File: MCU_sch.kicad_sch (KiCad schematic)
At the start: 10 parts

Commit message: WIP output stage
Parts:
- added R? (x2): 4.7k, symbol Device:R_US
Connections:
- net +3V3: now also R?.1, R?.1
- net DAC_SCL: now reaches IC?.17 (TCK/RPB8/SCL1/CTED10/PMD4/RB8)
- net DAC_SCL: now also R?.2
- net DAC_SDA: now reaches IC?.18 (TDO/RPB9/SDA1/CTED4/PMD3/RB9)
- net DAC_SDA: now also R?.2
- net PCM_BCLK: now reaches IC?.25 (CVREFOUT/AN10/C3INB/RPB14/SCK1/CTED5/PMWR/RB14)
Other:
- moved on the sheet: C?, R?

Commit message: Adding values to output stage
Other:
- title: (none) -> PIC32 Interface
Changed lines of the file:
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@@
 (kicad_sch (version 20211123) (generator eeschema)
   (paper "A4")
+  (title_block
+    (title "PIC32 Interface")
+  )
   (junction (at 27.94 48.26) (diameter 0) (color 0 0 0 0)
   )

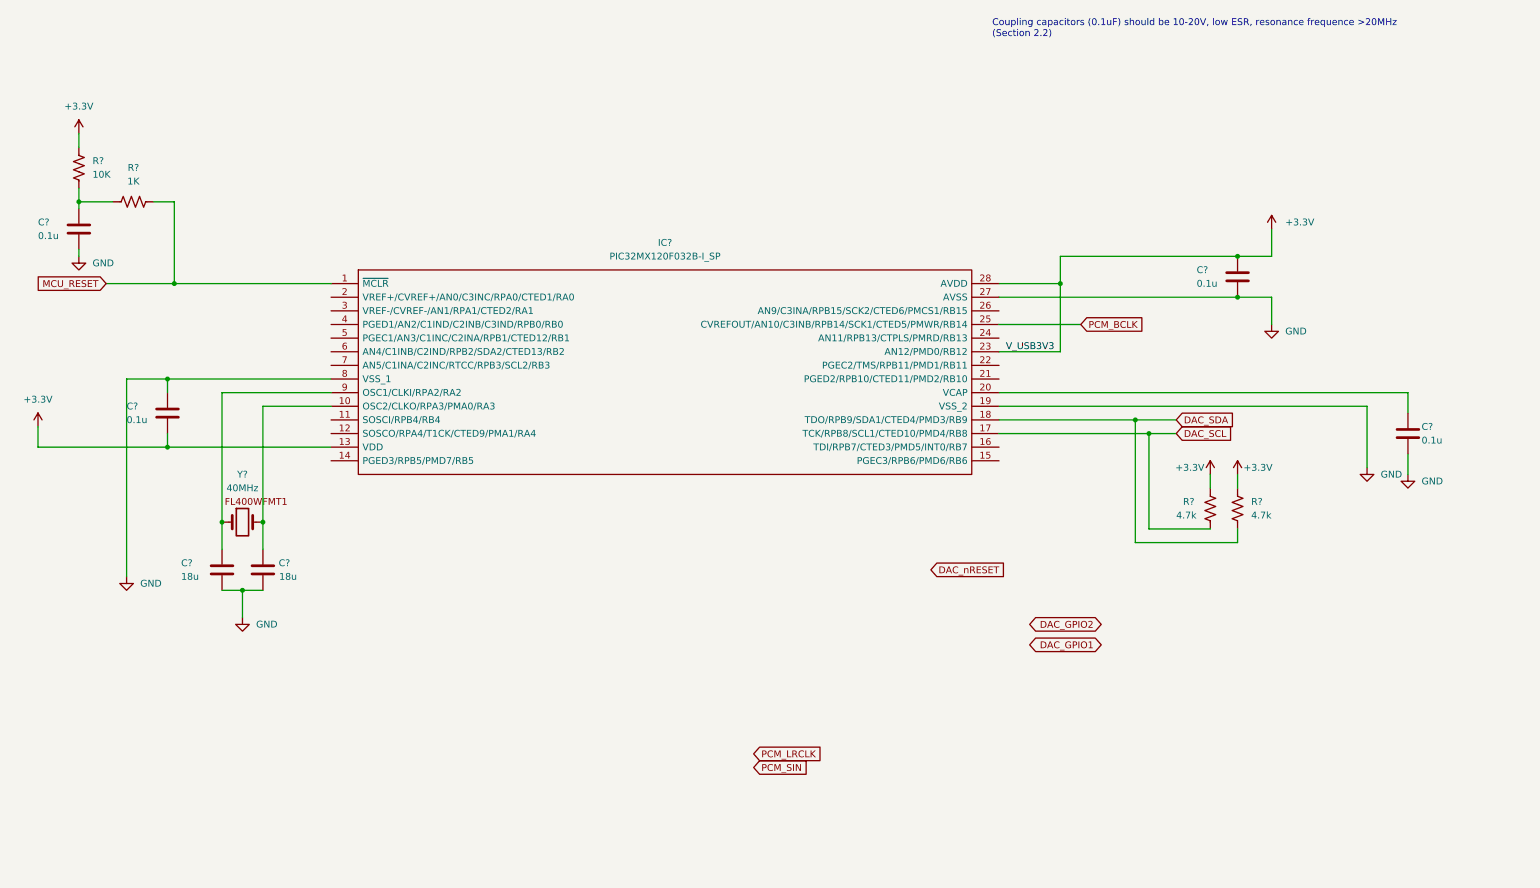
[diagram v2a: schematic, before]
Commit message: Redoing power stage and changing output stage accordingly
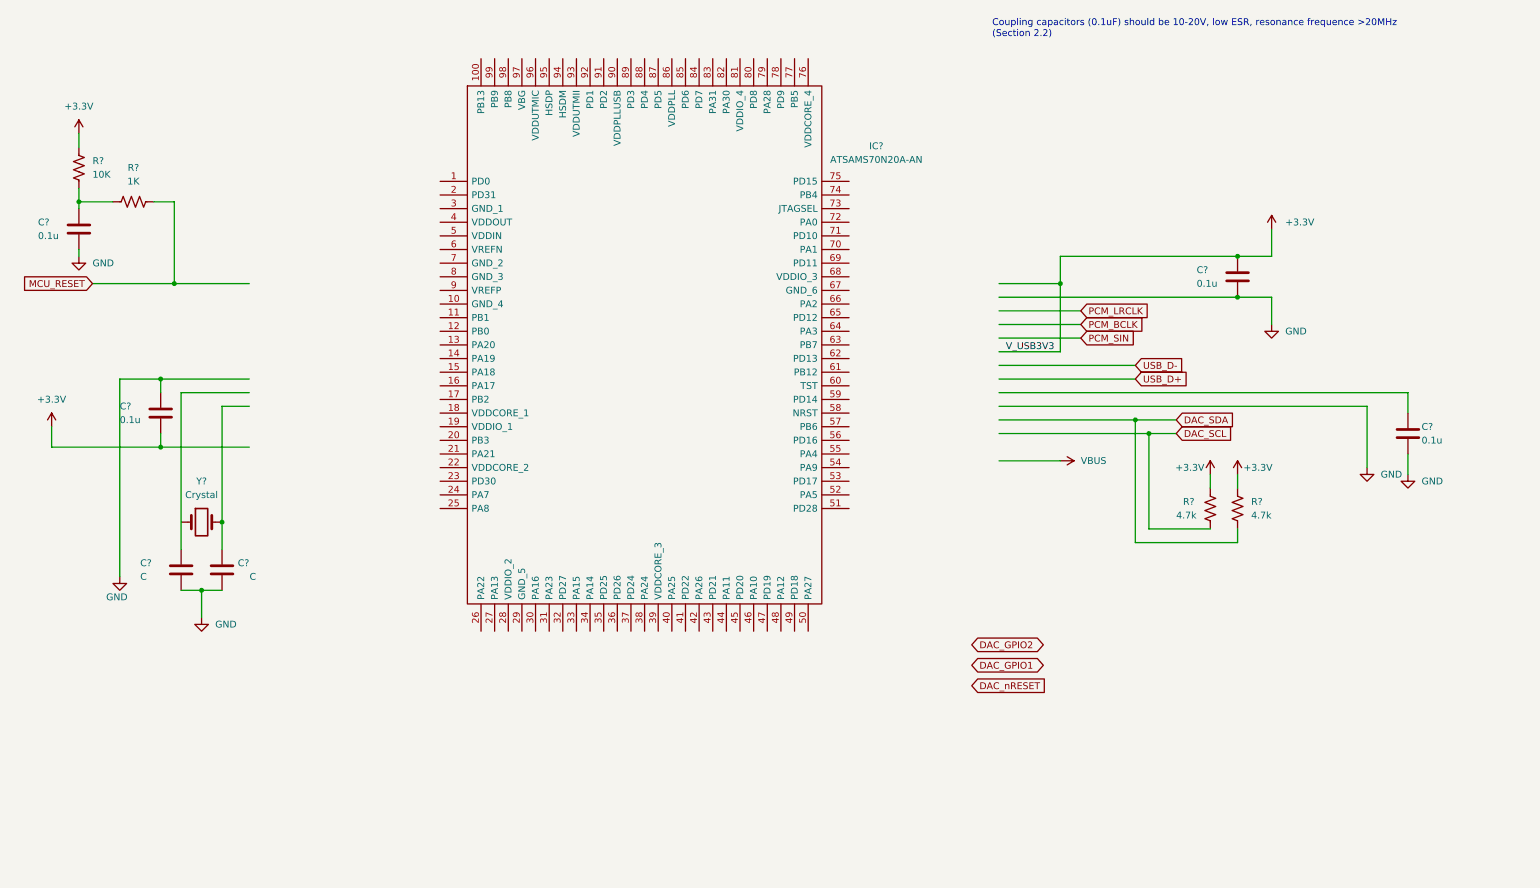
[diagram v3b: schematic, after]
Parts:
- removed IC?: PIC32MX120F032B-I_SP, DIP794W56P254L3486H508Q28N, symbol SamacSys_Parts:PIC32MX120F032B-I_SP
- removed Y?: 40MHz, symbol Device:Crystal
- added IC?: ATSAMS70N20A-AN, QFP50P1600X1600X160-100N, symbol SamacSys_Parts:ATSAMS70N20A-AN
- added Y?: Crystal, symbol Device:Crystal
- C? (x2): value 18u -> C
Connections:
- net at C?.2: now also Y?.2
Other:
- moved on the sheet: C?

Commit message: Finishing MCU interface. Adding connectors
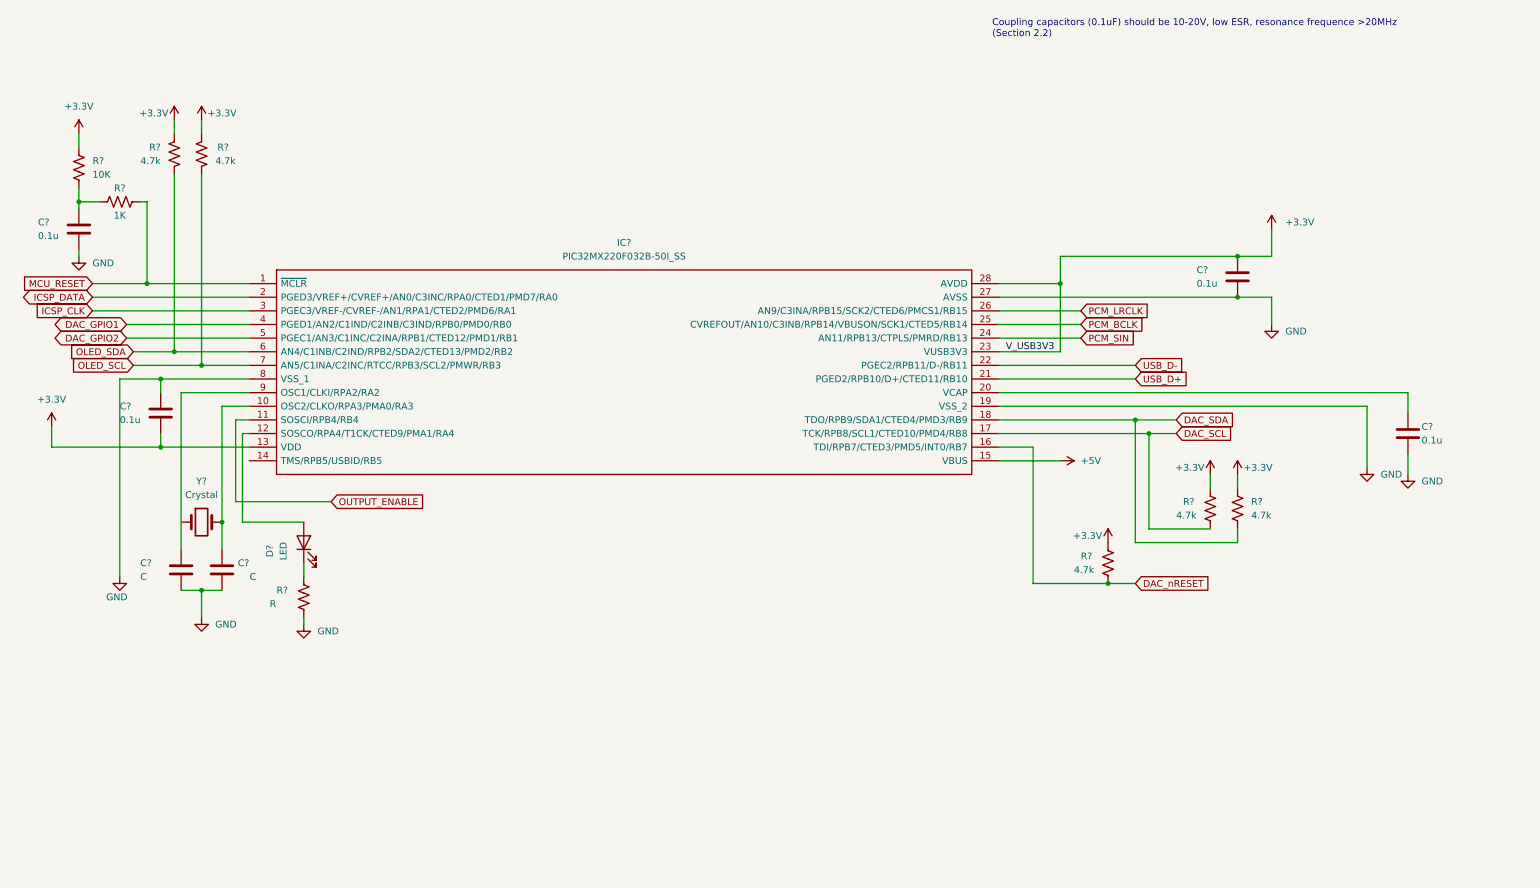
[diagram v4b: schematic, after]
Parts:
- removed IC?: ATSAMS70N20A-AN, QFP50P1600X1600X160-100N, symbol SamacSys_Parts:ATSAMS70N20A-AN
- added D?: LED, symbol Device:LED
- added IC?: PIC32MX220F032B-50I_SS, SOP65P780X200-28N, symbol SamacSys_Parts:PIC32MX220F032B-50I_SS
- added R? (x3): 4.7k, symbol Device:R_US
- added R?: R, symbol Device:R_US
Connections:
- net +3V3: now also IC?.13 (VDD), IC?.23 (VUSB3V3), IC?.28 (AVDD), R?.1, R?.1, R?.1
- net DAC_GPIO1: now also IC?.4 (PGED1/AN2/C1IND/C2INB/C3IND/RPB0/PMD0/RB0)
- net DAC_GPIO2: now also IC?.5 (PGEC1/AN3/C1INC/C2INA/RPB1/CTED12/PMD1/RB1)
- net DAC_SCL: now also IC?.17 (TCK/RPB8/SCL1/CTED10/PMD4/RB8)
- net DAC_SDA: now also IC?.18 (TDO/RPB9/SDA1/CTED4/PMD3/RB9)
- net DAC_nRESET: now also IC?.16 (TDI/RPB7/CTED3/PMD5/INT0/RB7), R?.2
- net GND: now also IC?.19 (VSS_2), IC?.27 (AVSS), IC?.8 (VSS_1), R?.2
- net MCU_RESET: now also IC?.1 (~{MCLR})
- net PCM_BCLK: now also IC?.25 (CVREFOUT/AN10/C3INB/RPB14/VBUSON/SCK1/CTED5/RB14)
- net PCM_LRCLK: now also IC?.26 (AN9/C3INA/RPB15/SCK2/CTED6/PMCS1/RB15)
- net PCM_SIN: now also IC?.24 (AN11/RPB13/CTPLS/PMRD/RB13)
- net USB_D+: now also IC?.21 (PGED2/RPB10/D+/CTED11/RB10)
- net USB_D-: now also IC?.22 (PGEC2/RPB11/D-/RB11)
- net at C?.2, Y?.2: now also IC?.10 (OSC2/CLKO/RPA3/PMA0/RA3)
- net at C?.1: now also IC?.9 (OSC1/CLKI/RPA2/RA2)
- net at C?.1: now also IC?.20 (VCAP)
- new net: D?.1 (K), R?.1
- new net: D?.2 (A), IC?.12 (SOSCO/RPA4/T1CK/CTED9/PMA1/RA4)
- new net +5V: IC?.15 (VBUS)
- new net ICSP_CLK: IC?.3 (PGEC3/VREF-/CVREF-/AN1/RPA1/CTED2/PMD6/RA1)
- new net ICSP_DATA: IC?.2 (PGED3/VREF+/CVREF+/AN0/C3INC/RPA0/CTED1/PMD7/RA0)
- new net OLED_SCL: IC?.7 (AN5/C1INA/C2INC/RTCC/RPB3/SCL2/PMWR/RB3), R?.2
- new net OLED_SDA: IC?.6 (AN4/C1INB/C2IND/RPB2/SDA2/CTED13/PMD2/RB2), R?.2
- new net OUTPUT_ENABLE: IC?.11 (SOSCI/RPB4/RB4)
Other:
- moved on the sheet: R?

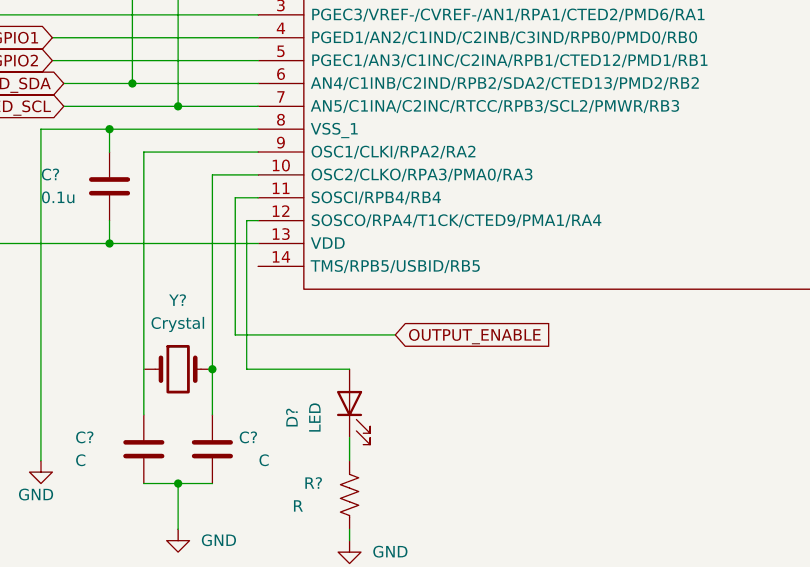
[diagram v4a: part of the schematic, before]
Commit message: Adding MCU LED
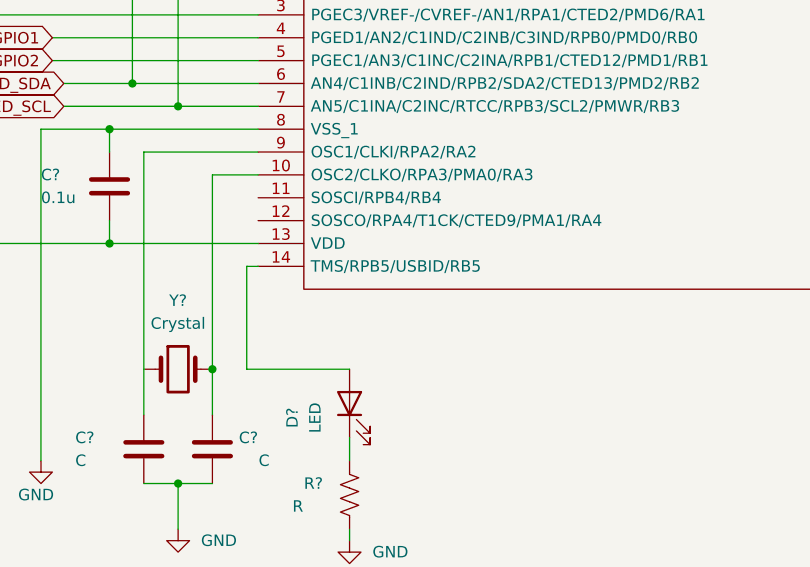
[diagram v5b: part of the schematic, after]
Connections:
- net at D?.2 (A): now also IC?.14 (TMS/RPB5/USBID/RB5); no longer IC?.12 (SOSCO/RPA4/T1CK/CTED9/PMA1/RA4)
- net OUTPUT_ENABLE: no longer names the net of IC?.11 (SOSCI/RPB4/RB4)
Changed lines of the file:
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@@
+    (stroke (width 0) (type default) (color 0 0 0 0))
+  )
+  (wire (pts (xy 58.42 96.52) (xy 58.42 107.95))
     (stroke (width 0) (type default) (color 0 0 0 0))
   )
@@
     (stroke (width 0) (type default) (color 0 0 0 0))
   )
+  (wire (pts (xy 275.59 99.06) (xy 275.59 95.25))
+    (stroke (width 0) (type default) (color 0 0 0 0))
+  )
+  (wire (pts (xy 205.74 119.38) (xy 219.71 119.38))
+    (stroke (width 0) (type default) (color 0 0 0 0))
+  )
+  (wire (pts (xy 243.84 101.6) (xy 243.84 99.06))
+    (stroke (width 0) (type default) (color 0 0 0 0))
+  )
+  (wire (pts (xy 36.83 71.12) (xy 59.69 71.12))
+    (stroke (width 0) (type default) (color 0 0 0 0))
+  )
+  (wire (pts (xy 27.94 57.15) (xy 27.94 58.42))
+    (stroke (width 0) (type default) (color 0 0 0 0))
+  )
+  (wire (pts (xy 50.8 78.74) (xy 59.69 78.74))
+    (stroke (width 0) (type default) (color 0 0 0 0))
+  )
+  (wire (pts (xy 205.74 119.38) (xy 205.74 93.98))
+    (stroke (width 0) (type default) (color 0 0 0 0))
+  )
+  (wire (pts (xy 227.33 109.22) (xy 227.33 91.44))
+    (stroke (width 0) (type default) (color 0 0 0 0))
+  )
+  (wire (pts (xy 27.94 35.56) (xy 27.94 38.1))
+    (stroke (width 0) (type default) (color 0 0 0 0))
+  )
+  (wire (pts (xy 69.85 115.57) (xy 69.85 118.11))
+    (stroke (width 0) (type default) (color 0 0 0 0))
+  )
+  (wire (pts (xy 267.97 97.79) (xy 267.97 86.36))
+    (stroke (width 0) (type default) (color 0 0 0 0))
+  )
+  (wire (pts (xy 36.83 73.66) (xy 59.69 73.66))
+    (stroke (width 0) (type default) (color 0 0 0 0))
+  )
+  (wire (pts (xy 199.39 68.58) (xy 214.63 68.58))
+    (stroke (width 0) (type default) (color 0 0 0 0))
+  )
+  (wire (pts (xy 50.8 120.65) (xy 54.61 120.65))
+    (stroke (width 0) (type default) (color 0 0 0 0))
+  )
+  (wire (pts (xy 30.48 63.5) (xy 40.64 63.5))
+    (stroke (width 0) (type default) (color 0 0 0 0))
+  )
+  (wire (pts (xy 199.39 66.04) (xy 243.84 66.04))
+    (stroke (width 0) (type default) (color 0 0 0 0))
+  )
+  (wire (pts (xy 38.1 76.2) (xy 45.72 76.2))
+    (stroke (width 0) (type default) (color 0 0 0 0))
+  )
   (wire (pts (xy 58.42 107.95) (xy 69.85 107.95))
     (stroke (width 0) (type default) (color 0 0 0 0))
   )
-  (wire (pts (xy 58.42 91.44) (xy 58.42 107.95))
-    (stroke (width 0) (type default) (color 0 0 0 0))
-  )
-  (wire (pts (xy 275.59 99.06) (xy 275.59 95.25))
-    (stroke (width 0) (type default) (color 0 0 0 0))
-  )
-  (wire (pts (xy 205.74 119.38) (xy 219.71 119.38))
-    (stroke (width 0) (type default) (color 0 0 0 0))
-  )
-  (wire (pts (xy 243.84 101.6) (xy 243.84 99.06))
-    (stroke (width 0) (type default) (color 0 0 0 0))
-  )
-  (wire (pts (xy 36.83 71.12) (xy 59.69 71.12))
-    (stroke (width 0) (type default) (color 0 0 0 0))
-  )
-  (wire (pts (xy 27.94 57.15) (xy 27.94 58.42))
-    (stroke (width 0) (type default) (color 0 0 0 0))
-  )
-  (wire (pts (xy 50.8 78.74) (xy 59.69 78.74))
-    (stroke (width 0) (type default) (color 0 0 0 0))
-  )
-  (wire (pts (xy 205.74 119.38) (xy 205.74 93.98))
-    (stroke (width 0) (type default) (color 0 0 0 0))
-  )
-  (wire (pts (xy 227.33 109.22) (xy 227.33 91.44))
-    (stroke (width 0) (type default) (color 0 0 0 0))
-  )
-  (wire (pts (xy 57.15 104.14) (xy 74.93 104.14))
-    (stroke (width 0) (type default) (color 0 0 0 0))
-  )
-  (wire (pts (xy 27.94 35.56) (xy 27.94 38.1))
-    (stroke (width 0) (type default) (color 0 0 0 0))
-  )
-  (wire (pts (xy 69.85 115.57) (xy 69.85 118.11))
-    (stroke (width 0) (type default) (color 0 0 0 0))
-  )
-  (wire (pts (xy 59.69 88.9) (xy 57.15 88.9))
-    (stroke (width 0) (type default) (color 0 0 0 0))
-  )
-  (wire (pts (xy 59.69 91.44) (xy 58.42 91.44))
-    (stroke (width 0) (type default) (color 0 0 0 0))
-  )
-  (wire (pts (xy 267.97 97.79) (xy 267.97 86.36))
-    (stroke (width 0) (type default) (color 0 0 0 0))
-  )
-  (wire (pts (xy 36.83 73.66) (xy 59.69 73.66))
-    (stroke (width 0) (type default) (color 0 0 0 0))
-  )
-  (wire (pts (xy 57.15 88.9) (xy 57.15 104.14))
-    (stroke (width 0) (type default) (color 0 0 0 0))
-  )
-  (wire (pts (xy 199.39 68.58) (xy 214.63 68.58))
-    (stroke (width 0) (type default) (color 0 0 0 0))
-  )
-  (wire (pts (xy 50.8 120.65) (xy 54.61 120.65))
-    (stroke (width 0) (type default) (color 0 0 0 0))
-  )
-  (wire (pts (xy 30.48 63.5) (xy 40.64 63.5))
-    (stroke (width 0) (type default) (color 0 0 0 0))
-  )
-  (wire (pts (xy 199.39 66.04) (xy 243.84 66.04))
-    (stroke (width 0) (type default) (color 0 0 0 0))
-  )
-  (wire (pts (xy 38.1 76.2) (xy 45.72 76.2))
-    (stroke (width 0) (type default) (color 0 0 0 0))
-  )
   (wire (pts (xy 35.56 81.28) (xy 35.56 118.11))
     (stroke (width 0) (type default) (color 0 0 0 0))
@@
   )
   (wire (pts (xy 199.39 86.36) (xy 267.97 86.36))
+    (stroke (width 0) (type default) (color 0 0 0 0))
+  )
+  (wire (pts (xy 58.42 96.52) (xy 59.69 96.52))
     (stroke (width 0) (type default) (color 0 0 0 0))
   )
@@
       (effects (font (size 1.27 1.27)) (justify left) hide)
     )
-  )
-  (global_label "OUTPUT_ENABLE" (shape input) (at 74.93 104.14 0) (fields_autoplaced)
-    (effects (font (size 1.27 1.27)) (justify left))
-    (property "Intersheet References" "${INTERSHEET_REFS}" (id 0) (at 92.5226 104.0606 0)
-      (effects (font (size 1.27 1.27)) (justify left) hide)
-    )
